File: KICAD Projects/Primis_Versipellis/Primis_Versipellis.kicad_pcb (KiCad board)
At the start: 2 copper layers, 50 x 26 mm, 31 parts, among them J1 USB-05, J3 Conn_01x05_Pin, U1 nRF52833_QDxx, Y2 Crystal_GND24

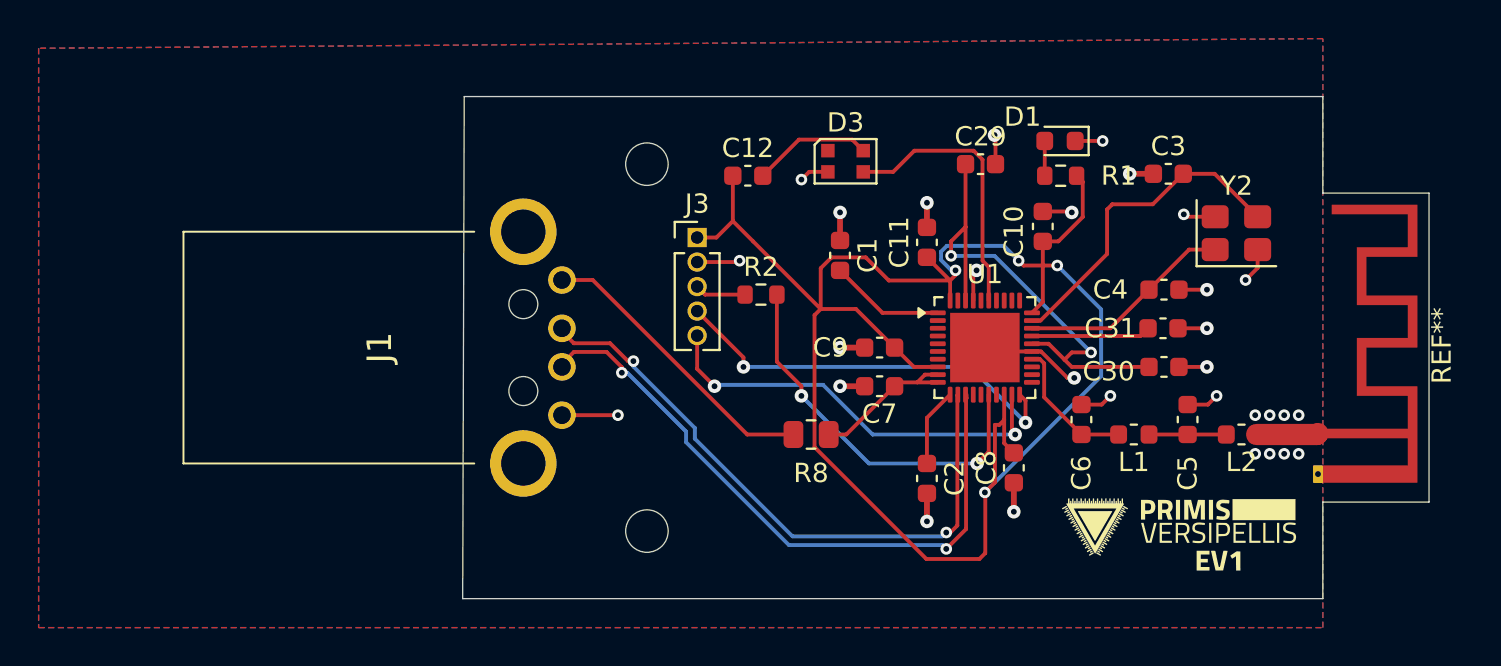
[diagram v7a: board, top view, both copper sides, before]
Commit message: VERSIPELLIS EV2 + TURRIM Production files
-Swapped to a tag connect for programming VERSIPELLIS
-Moved crystal closer to the NRF on VERSIPELLIS
-Fixed swapped lines on usb on VERSIPELLIS
-TURRIM cleanup and production files added
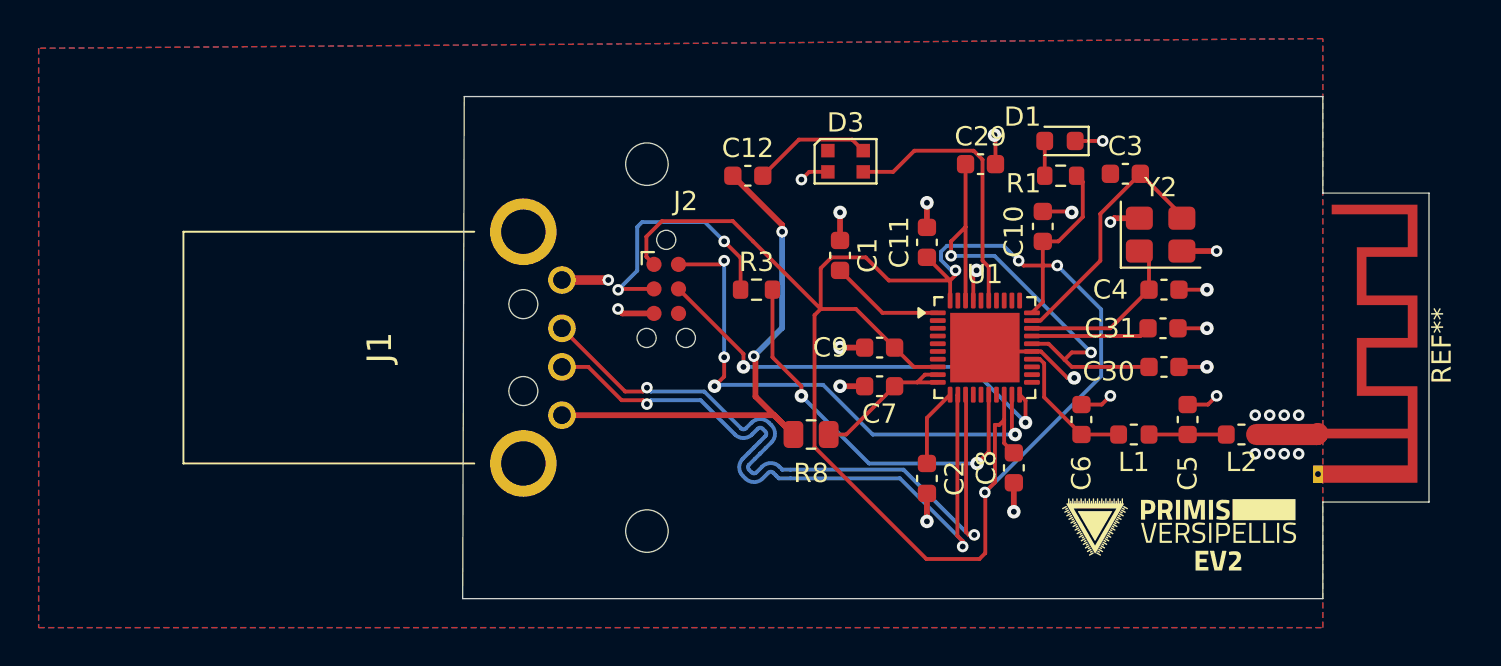
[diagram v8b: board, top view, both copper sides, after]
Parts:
- removed J3: Conn_01x05_Pin, Connector_PinHeader_1.27mm:PinHeader_1x05_P1.27mm_Vertical
- removed R2: 10k, Resistor_SMD:R_0603_1608Metric
- added G***: LOGO, LOGO, B.Cu at (162.5, 69.8)
- added G***: LOGO, LOGO, B.Cu at (157.0, 80.0)
- added J2: Conn_ARM_SWD_TagConnect_TC2030-NL, Connector:Tag-Connect_TC2030-IDC-NL_2x03_P1.27mm_Vertical, F.Cu at (135.0, 66.5)
- added R3: 10k, Resistor_SMD:R_0603_1608Metric, F.Cu at (139.7, 66.5)
- moved Y2 3.93 mm to (160.6, 63.6)
- moved C3 2.22 mm to (158.8, 60.5)
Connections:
- C12 pad 1: VDD_nRF -> VBUS
- J1 pad 1: VBUS -> GND
- J1 pad 2: D- -> D+
- J1 pad 3: D+ -> D-
- J1 pad 4: GND -> VBUS
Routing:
- net Net-(J2-~{RESET}): track 0.00 -> 13.4 mm, vias 0 -> 2
- net VBUS: track 15.7 -> 28.3 mm, vias 0 -> 2
- net Net-(J2-SWDIO): track 21.8 -> 27.9 mm, vias 2 -> 4
- net D-: track 32.6 -> 36.7 mm
- net Net-(U1-XC2): track 17.1 -> 13.4 mm
- net D+: track 33.7 -> 37.3 mm
- net Net-(J3-Pin_3): track 2.65 -> 0.00 mm
- net GND: track 38.9 -> 36.7 mm, vias 30 -> 29
- net Net-(U1-XC1): track 11.3 -> 9.10 mm
- net VDD_nRF: track 92.5 -> 94.3 mm
- net Net-(J2-SWCLK): track 21.2 -> 22.8 mm
